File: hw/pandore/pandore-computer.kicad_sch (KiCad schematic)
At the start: 1 part

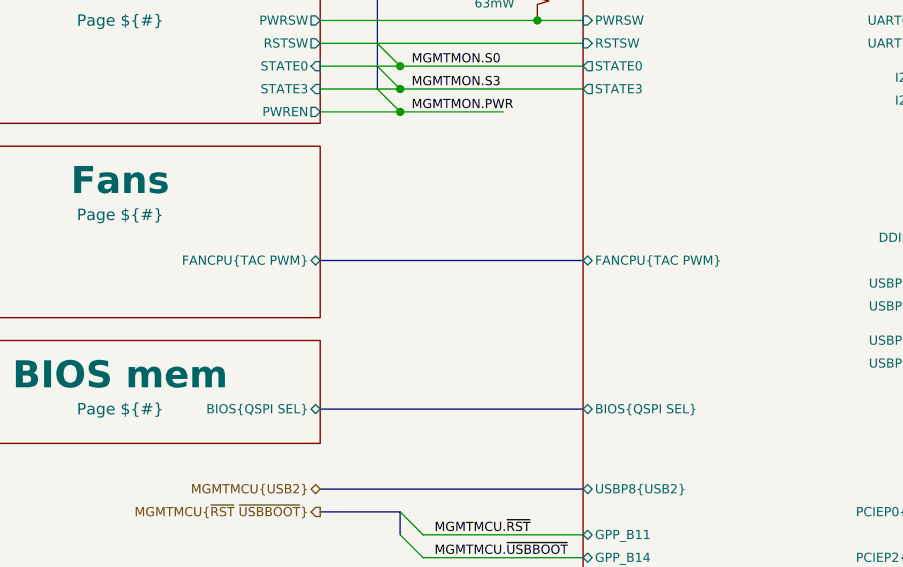
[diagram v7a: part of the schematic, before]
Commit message: more routing/placement done added 5v load switch 1A each added second fan circuit redone all diffpair routing following new stackup calc added all (?) missing connectors to unused pins
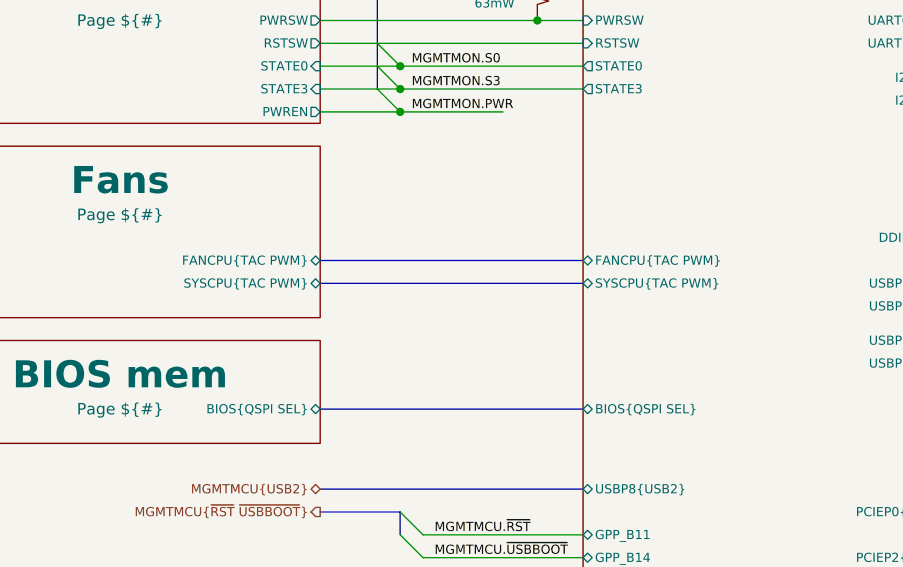
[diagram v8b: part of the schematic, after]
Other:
- sheet Computer module ports: added SYSCPU{TAC PWM}; removed none
- sheet Fans ports: added SYSCPU{TAC PWM}; removed none
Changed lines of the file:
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@@
+	(bus
+		(pts
+			(xy 92.71 93.98) (xy 121.92 93.98)
+		)
+		(stroke
+			(width 0)
+			(type default)
+		)
+	)
 	(bus
 		(pts
@@
 			)
 		)
+		(pin "SYSCPU{TAC PWM}" bidirectional
+			(at 121.92 93.98 180)
+			(effects
+				(font
+					(size 1.016 1.016)
+				)
+				(justify left)
+			)
+		)
 		(instances
 			(project "pandore"
@@
 			(effects
 				(font
+					(size 1.016 1.016)
+				)
+				(justify right)
+			)
+		)
+		(pin "SYSCPU{TAC PWM}" bidirectional
+			(at 92.71 93.98 0)
+			(effects
+				(font
